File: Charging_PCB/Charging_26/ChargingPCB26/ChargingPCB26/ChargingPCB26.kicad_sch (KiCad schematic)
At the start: 48 parts, among them J1 Molex6pin, J2 Molex6pin, K101 Relay_SPDT_Omron_G2RL-1, K102 Relay_SPDT_Omron_G2RL-1, Q1 NMOS, Q103 Q_NPN_BEC, Q104 Q_NPN_BEC, Q105 Q_NPN_BEC, Q106 Q_NPN_BEC, Q2 NMOS, SW101 SW_Omron_B3FS, SW102 SW_Omron_B3FS, U1 SFH617A-1, U107 LM7805_TO220, U2 SFH617A-1, U5 74LS279, U6 74HC00

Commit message: charging pcb layout
charging pcb ready to order, would like funny logo on there
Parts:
- added D3: LED, LED_SMD:LED_0805_2012Metric_Pad1.15x1.40mm_HandSolder, symbol Device:LED
- added D4: D_Schottky, Diode_SMD:D_SMA, symbol Device:D_Schottky
- added Q3, Q4: NMOS, Package_TO_SOT_THT:TO-251-3_Vertical, symbol Simulation_SPICE:NMOS
- added R10, R8: 10k, Resistor_SMD:R_0805_2012Metric_Pad1.20x1.40mm_HandSolder, symbol Device:R_US
- added R11, R12: 100, Resistor_SMD:R_0805_2012Metric_Pad1.20x1.40mm_HandSolder, symbol Device:R_US
- added R7: 1k, Resistor_SMD:R_0805_2012Metric_Pad1.20x1.40mm_HandSolder, symbol Device:R_US
- added R9: 500, Resistor_SMD:R_0805_2012Metric_Pad1.20x1.40mm_HandSolder, symbol Device:R_US
- C101, C102, C106: footprint Capacitor_THT:CP_Radial_D5.0mm_P2.50mm -> Capacitor_SMD:C_0402_1005Metric; JLC# (none) -> C15195; MPN (none) -> CL05B103KB5NNNC
- C105: footprint Capacitor_THT:CP_Radial_D5.0mm_P2.50mm -> Capacitor_SMD:C_0402_1005Metric; JLC# (none) -> C107013; MPN (none) -> CC0402KRX5R6BB334
- C117, C3: footprint Capacitor_THT:CP_Radial_D5.0mm_P2.50mm -> Capacitor_SMD:C_0603_1608Metric_Pad1.08x0.95mm_HandSolder; JLC# (none) -> C1591; MPN (none) -> CL10B104KB8NNNC
- D1, D2: footprint LED_THT:LED_D3.0mm -> LED_SMD:LED_0805_2012Metric_Pad1.15x1.40mm_HandSolder; JLC# (none) -> C84256; MPN (none) -> NCD0805R1
- D101, D102: footprint Diode_THT:D_DO-201AD_P12.70mm_Horizontal -> Diode_SMD:D_SMA; JLC# (none) -> C8678; MPN (none) -> SS34
- F1: footprint (none) -> Fuse:Fuseholder_Blade_Mini_Keystone_3568; Digikey (none) -> 36-3568-ND
- H101, H102, H103, H104: footprint (none) -> MountingHole:MountingHole_2.2mm_M2
- J1, J2: footprint Connector_Molex:Molex_Mini-Fit_Jr_5566-06A_2x03_P4.20mm_Vertical -> Connector_Molex:Molex_Nano-Fit_105314-xx06_2x03_P2.50mm_Horizontal; JLC# (none) -> C586245; MPN (none) -> 1053141106
- K101, K102: JLC# (none) -> C469130; MPN (none) -> G2RL-1-DC12
- Q1, Q2: JLC# (none) -> C3278986; MPN (none) -> IPU60R2K1CEAKMA1
- Q103, Q104, Q105, Q106: footprint Package_TO_SOT_THT:TO-92 -> Package_TO_SOT_SMD:SOT-23; JLC# (none) -> C2146; MPN (none) -> S8050 J3Y(RANGE:200-350)
- R1, R105, R106, R2: footprint Resistor_THT:R_Axial_DIN0207_L6.3mm_D2.5mm_P7.62mm_Horizontal -> Resistor_SMD:R_0805_2012Metric_Pad1.20x1.40mm_HandSolder; JLC# (none) -> C17414; MPN (none) -> 0805W8F1002T5E
- R103, R104, R110, R112: footprint Resistor_THT:R_Axial_DIN0207_L6.3mm_D2.5mm_P7.62mm_Horizontal -> Resistor_SMD:R_0805_2012Metric_Pad1.20x1.40mm_HandSolder; JLC# (none) -> C149504; MPN (none) -> 0805W8F1003T5E
- R108, R109, R111, R113: footprint Resistor_THT:R_Axial_DIN0207_L6.3mm_D2.5mm_P7.62mm_Horizontal -> Resistor_SMD:R_0805_2012Metric_Pad1.20x1.40mm_HandSolder; JLC# (none) -> C17513; MPN (none) -> 0805W8F1001T5E
- R3, R4: value 2k -> 500; footprint Resistor_THT:R_Axial_DIN0207_L6.3mm_D2.5mm_P7.62mm_Horizontal -> Resistor_SMD:R_0805_2012Metric_Pad1.20x1.40mm_HandSolder; JLC# (none) -> C2828711; MPN (none) -> ARG05BTC5000
- R5, R6: value 10k -> 1k; footprint Resistor_THT:R_Axial_DIN0207_L6.3mm_D2.5mm_P7.62mm_Horizontal -> Resistor_SMD:R_0805_2012Metric_Pad1.20x1.40mm_HandSolder; JLC# (none) -> C17513; MPN (none) -> 0805W8F1001T5E
- SW101, SW102: footprint Button_Switch_THT:SW_PUSH_6mm_H4.3mm -> Button_Switch_SMD:SW_SPST_Omron_B3FS-100xP; JLC# (none) -> C271750; MPN (none) -> B3FS-1000P
- U1, U2: JLC# (none) -> C5350; MPN (none) -> PC817X2NSZW
- U107: JLC# (none) -> C71107; MPN (none) -> LM7805L-TF3-T
- U5: JLC# (none) -> C41430933; MPN (none) -> SN74LS279AN
- U6: JLC# (none) -> C2902; MPN (none) -> SN74HC00N
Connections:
- net +12V: now also D4.1 (K), R7.1
- net +5V: now also R9.1
- net BMS_CSO: now also R7.2
- net GND: now also J2.4 (Pin_4), Q3.3 (S), Q4.3 (S), R10.2, R8.2; no longer J1.4 (Pin_4)
- net +12_Shutdown renamed Charger_SHDN
- net Charger_SHDN: now also R10.1, R11.1, R12.1, R8.1
- new net: D3.1 (K), Q3.1 (D)
- new net: Q3.2 (G), R12.2
- new net: D3.2 (A), R9.2
- new net: Q4.2 (G), R11.2
- new net -12V_Contactor: D4.2 (A), J1.4 (Pin_4), Q4.1 (D)
- no-connect marks 17 -> 16
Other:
- note added: "Power Connections"
- note added: "Signal Connections/Accumulator Power"
- moved on the sheet: C101, C102, C105, C106, C117, C3, D1, D101, D102, D2, F1, H101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

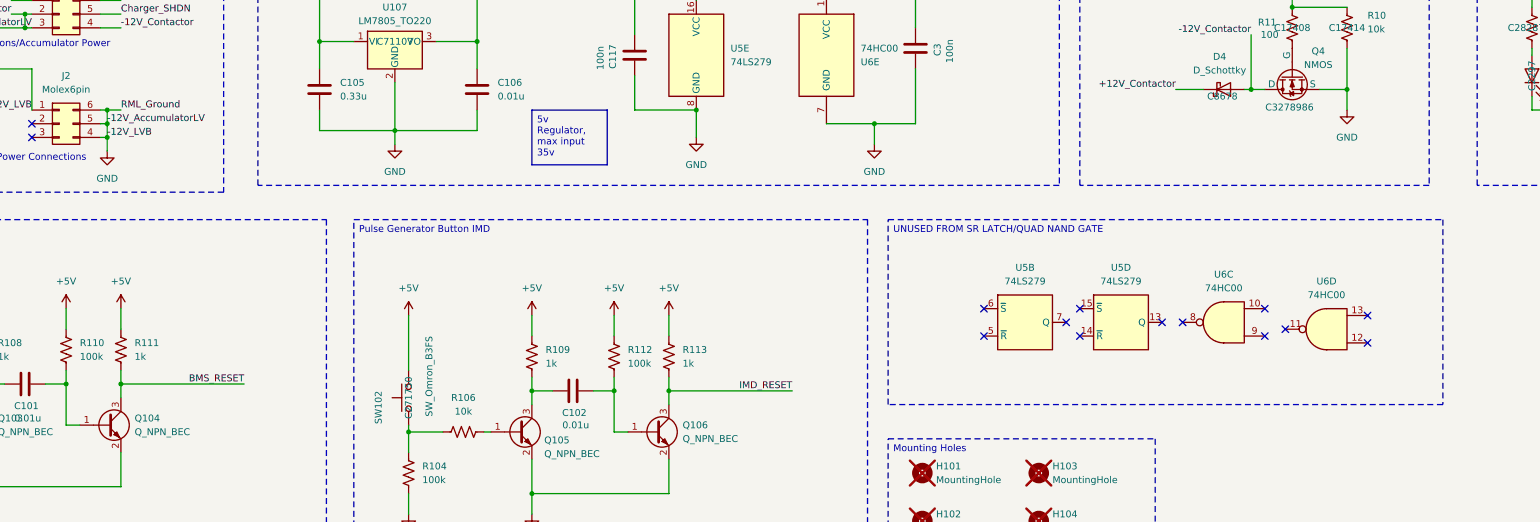
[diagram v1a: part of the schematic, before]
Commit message: charging pcb
terminated unused SR latch/Nand gate inputs
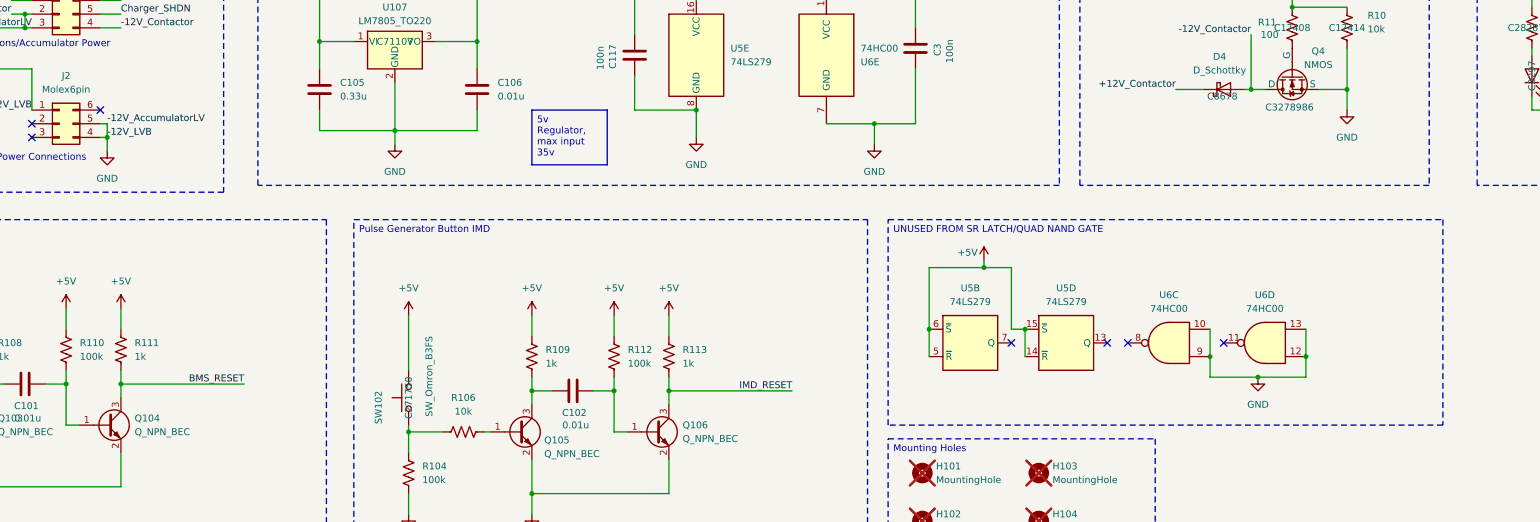
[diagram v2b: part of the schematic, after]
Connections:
- net +5V: now also U5.14 (~{R}), U5.15 (~{S}), U5.5 (~{R}), U5.6 (~{S})
- net GND: now also U6.10, U6.12, U6.13, U6.9; no longer J2.6 (Pin_6)
- no-connect marks 16 -> 9
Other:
- moved on the sheet: U5B, U5D, U6C, U6D

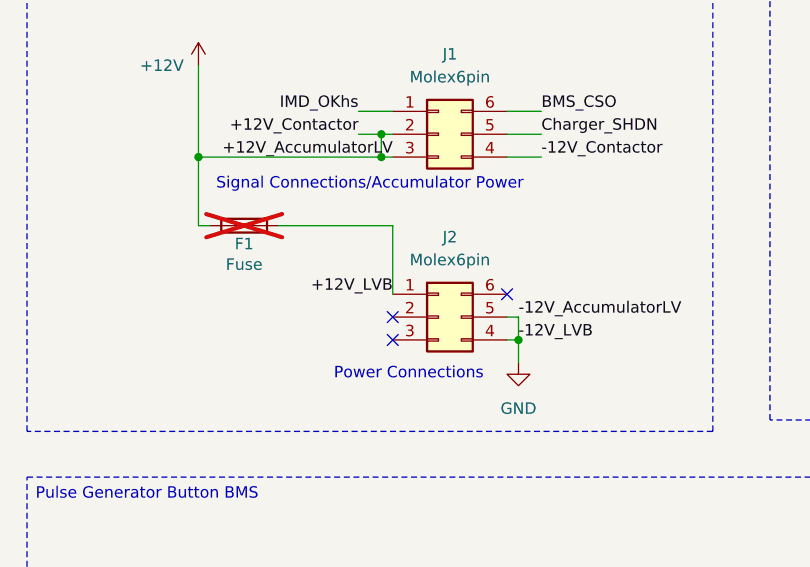
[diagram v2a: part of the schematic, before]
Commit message: precharge/discharge. charging
removed discharge ffrom precharge and put it on board out of battery, updqted charging according to discharge
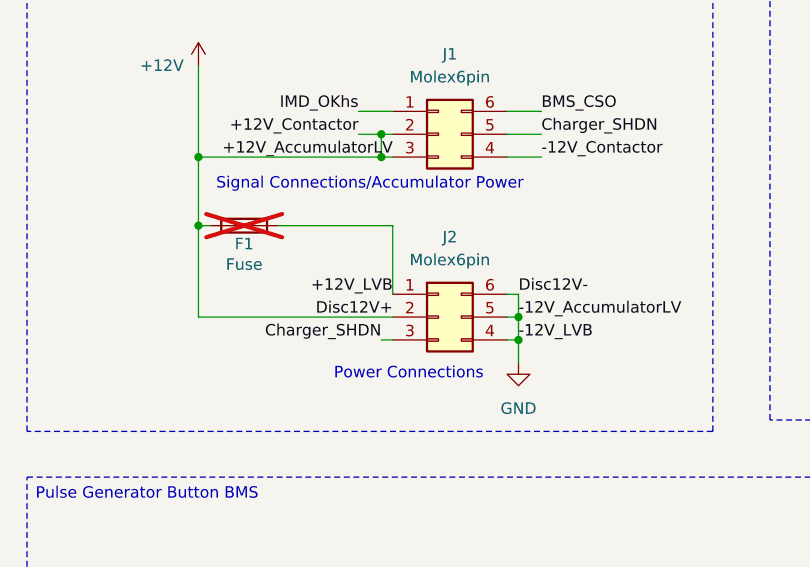
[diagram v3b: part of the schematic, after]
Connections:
- net +12V: now also J2.2 (Pin_2)
- net Charger_SHDN: now also J2.3 (Pin_3)
- net GND: now also J2.6 (Pin_6)
- no-connect marks 9 -> 6
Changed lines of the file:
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@@
 	)
 	(junction
+		(at 85.09 215.9)
+		(diameter 0)
+		(color 0 0 0 0)
+	)
+	(junction
 		(at 105.41 100.33)
 		(diameter 0)
@@
 	)
 	(junction
+		(at 49.53 205.74)
+		(diameter 0)
+		(color 0 0 0 0)
+	)
+	(junction
 		(at 237.49 254)
 		(diameter 0)
@@
 	)
 	(no_connect
-		(at 71.12 218.44)
-	)
-	(no_connect
 		(at 320.04 138.43)
 	)
@@
 	)
 	(no_connect
-		(at 71.12 215.9)
-	)
-	(no_connect
-		(at 83.82 213.36)
-	)
-	(no_connect
 		(at 292.1 256.54)
 	)
@@
 	(wire
 		(pts
+			(xy 71.12 215.9) (xy 49.53 215.9)
+		)
+		(stroke
+			(width 0)
+			(type default)
+		)
+	)
+	(wire
+		(pts
 			(xy 138.43 217.17) (xy 138.43 219.71)
 		)
@@
 	(wire
 		(pts
+			(xy 69.85 218.44) (xy 71.12 218.44)
+		)
+		(stroke
+			(width 0)
+			(type default)
+		)
+	)
+	(wire
+		(pts
+			(xy 85.09 213.36) (xy 85.09 215.9)
+		)
+		(stroke
+			(width 0)
+			(type default)
+		)
+	)
+	(wire
+		(pts
 			(xy 317.5 118.11) (xy 323.85 118.11)
 		)
@@
 	(wire
 		(pts
+			(xy 83.82 213.36) (xy 85.09 213.36)
+		)
+		(stroke
+			(width 0)
+			(type default)
+		)
+	)
+	(wire
+		(pts
 			(xy 234.95 205.74) (xy 234.95 215.9)
 		)
@@
 	(wire
 		(pts
+			(xy 49.53 215.9) (xy 49.53 205.74)
+		)
+		(stroke
+			(width 0)
+			(type default)
+		)
+	)
+	(wire
+		(pts
 			(xy 317.5 130.81) (xy 317.5 118.11)
 		)
@@
 		)
 	)
+	(label "Charger_SHDN"
+		(at 69.85 218.44 180)
+		(effects
+			(font
+				(size 1.27 1.27)
+			)
+			(justify right bottom)
+		)
+	)
 	(label "+12V_Contactor"
 		(at 283.21 209.55 180)
@@
 		)
 	)
+	(label "Disc12V+"
+		(at 71.12 215.9 180)
+		(effects
+			(font
+				(size 1.27 1.27)
+			)
+			(justify right bottom)
+		)
+	)
 	(label "IMD_RESET"
 		(at 212.09 265.43 180)
@@
 		(effects
 			(font
+				(size 1.27 1.27)
+			)
+			(justify left bottom)
+		)
+	)
+	(label "Disc12V-"
+		(at 85.09 213.36 0)
+		(effects
+			(font

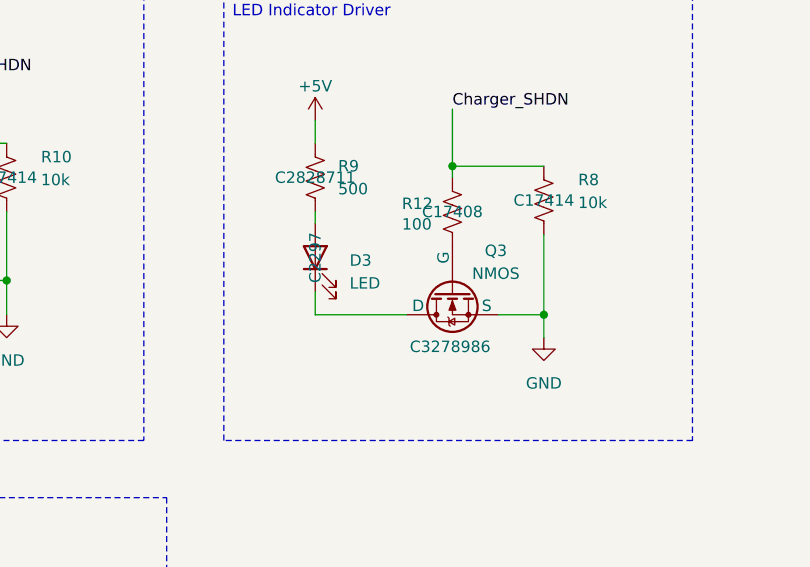
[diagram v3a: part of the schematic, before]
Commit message: BSPD, Precharge, and Charging PCB BOMs pulled
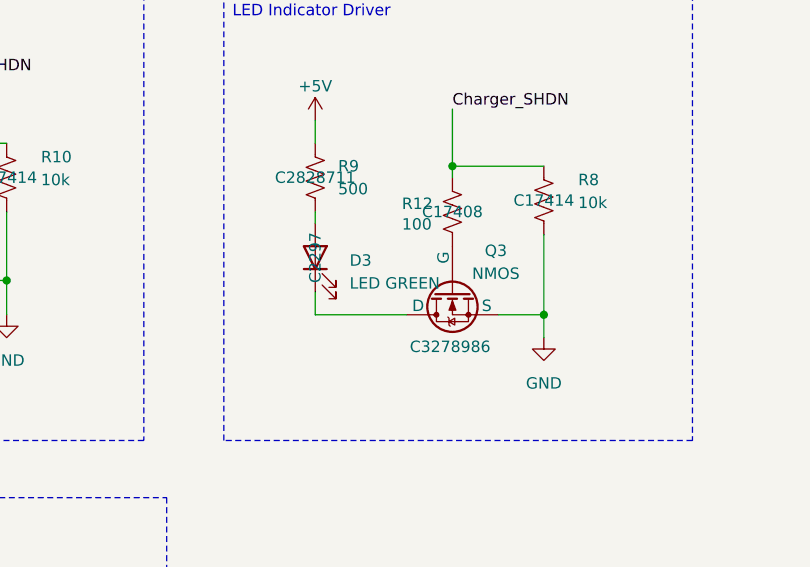
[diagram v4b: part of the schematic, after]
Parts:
- D3: value LED -> LED GREEN; Digikey 516-1313-ND -> (none)
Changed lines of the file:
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@@
 			"AAAAAAAAAAAAAAAAAAAAAAAAAAAAAAAAAAAAAAAAAAAAAAAAAAAAAAAAAAAAAAAAAAAAAAAAAAAA"
 			"AAAAAAAAAAAAAAAAAAAAAAAAAAAAAAAAAAAAAAAAAAAAAAAAAAAAAAAAAAAAAAAAAAAAAAAAAAAA"
+			"AAAAAAAAAAAAAAAAAAAAAAAAAAAAAAAAAAAAAAAAAAAAAAAAAAAAAAAAAAAAAAAAAAAAAAAAAAAA"
+			"AAAAAAAAAAAAAAAAAAAAAAAAAAAAAAAAAAAAAAAAAAAAAAAAAAAAAAAAAAAAAAAAAAAAAAAAAAAA"
+			"AAAAAAAAAAAAAAAAAAAAAAAAAAAAAAAAAAAAAAAAAAAAAAAAAAAAAAAAAAAAAAAAAAAAAAAAAAAA"
+			"AAAAAAAAAAAAAAAAAAAAAAAAAAAAAAAAAAAAAAAAAAAAAAAAAAAAAAAAAAAAAAAAAAAAAAAAAAAA"
+			"AAAAAAAAAAAAAAAAAAAAAAAAAAAAAAAAAAAAAAAAAAAAAAAAAAAAAAAAAAAAAAAAAAAAAAAAAAAA"
+			"AAAAAAAAAAAAAAAAAAAAAAAAAAAAAAAAAAAAAAAAAAAAAAAAAAAAAAAAAAAAAAAAAAAAAAAAAAAA"
+			"AAAAAAAAAAAAAAAAAAAAAAAAAAAAAAAAAAAAAAAAAAAAAAAAAAAAAAAAAAAAAAAAAAAAAAAAAAAA"
+			"AAAAAAAAAAAAAAAAAAAAAAAAAAAAAAAAAAAAAAAAAAAAAAAAAAAAAAAAAAAAAAAAAAAAAAAAAAAA"
+			"AAAAAAAAAAAAAAAAAAAAAAAAAAAAAAAAAAAAAAAAAAAAAAAAAAAAAAAAAAAAAAAAAAAAAAAAAAAA"
+			"AAAAAAAAAAAAAAAAAAAAAAAAAAAAAAAAAAAAAAAAAAAAAAAAAAAAAAAAAAAAAAAAAAAAAAAAAAAA"
+			"AAAAAAAAAAAAAAAAAAAAAAAAAAAAAAAAAAAAAAAAAAAAAAAAAAAAAAAAAAAAAAAAAAAAAAAAAAAA"
+			"AAAAAAAAAAAAAAAAAAAAAAAAAAAAAAAAAAAAAAAAAAAAAAAAAAAAAAAAAAAAAAAAAAAAAAAAAAAA"
+			"AAAAAAAAAAAAAAAAAAAAAAAAAAAAAAAAAAAAAAAAAAAAAAAAAAAAAAAAAAAAAAAAAAAAAAAAAAAA"
+			"AAAAAAAAAAAAAAAAAAAAAAAAAAAAAAAAAAAAAAAAAAAAAAAAAAAAAAAAAAAAAAAAAAAAAAAAAAAA"
+			"AAAAAAAAAAAAAAAAAAAAAAAAAAAAAAAAAAAAAAAAAAAAAAAAAAAAAAAAAAAAAAAAAAAAAAAAAAAA"
+			"AAAAAAAAAAAAAAAAAAAAAAAAAAAAAAAAAAAAAAAAAAAAAAAAAAAAAAAAAAAAAAAAAAAAAAAAAAAA"
+			"AAAAAAAAAAAAAAAAAAAAAAAAAAAAAAAAAAAAAAAAAAAAAAAAAAAAAAAAAAAAAAAAAAAAAAAAAAAA"
+			"AAAAAAAAAAAAAAAAAAAAAAAAAAAAAAAAAAAAAAAAAAAAAAAAAAAAAAAAAAAAAAAAAAAAAAAAAAAA"
 			"AAAAAAAAAAAAAA=="
 		)
@@
 			"AAAAAAAAAAAAAAAAAAAAAAAAAAAAAAAAAAAAAAAAAAAAAAAAAAAAAAAAAAAAAAAAAAAAAAAAAAAA"
 			"AAAAAAAAAAAAAAAAAAAAAAAAAAAAAAAAAAAAAAAAAAAAAAAAAAAAAAAAAAAAAAAAAAAAAAAAAAAA"
+			"AAAAAAAAAAAAAAAAAAAAAAAAAAAAAAAAAAAAAAAAAAAAAAAAAAAAAAAAAAAAAAAAAAAAAAAAAAAA"
+			"AAAAAAAAAAAAAAAAAAAAAAAAAAAAAAAAAAAAAAAAAAAAAAAAAAAAAAAAAAAAAAAAAAAAAAAAAAAA"
+			"AAAAAAAAAAAAAAAAAAAAAAAAAAAAAAAAAAAAAAAAAAAAAAAAAAAAAAAAAAAAAAAAAAAAAAAAAAAA"
+			"AAAAAAAAAAAAAAAAAAAAAAAAAAAAAAAAAAAAAAAAAAAAAAAAAAAAAAAAAAAAAAAAAAAAAAAAAAAA"
+			"AAAAAAAAAAAAAAAAAAAAAAAAAAAAAAAAAAAAAAAAAAAAAAAAAAAAAAAAAAAAAAAAAAAAAAAAAAAA"
+			"AAAAAAAAAAAAAAAAAAAAAAAAAAAAAAAAAAAAAAAAAAAAAAAAAAAAAAAAAAAAAAAAAAAAAAAAAAAA"
+			"AAAAAAAAAAAAAAAAAAAAAAAAAAAAAAAAAAAAAAAAAAAAAAAAAAAAAAAAAAAAAAAAAAAAAAAAAAAA"
+			"AAAAAAAAAAAAAAAAAAAAAAAAAAAAAAAAAAAAAAAAAAAAAAAAAAAAAAAAAAAAAAAAAAAAAAAAAAAA"
+			"AAAAAAAAAAAAAAAAAAAAAAAAAAAAAAAAAAAAAAAAAAAAAAAAAAAAAAAAAAAAAAAAAAAAAAAAAAAA"
+			"AAAAAAAAAAAAAAAAAAAAAAAAAAAAAAAAAAAAAAAAAAAAAAAAAAAAAAAAAAAAAAAAAAAAAAAAAAAA"
+			"AAAAAAAAAAAAAAAAAAAAAAAAAAAAAAAAAAAAAAAAAAAAAAAAAAAAAAAAAAAAAAAAAAAAAAAAAAAA"
+			"AAAAAAAAAAAAAAAAAAAAAAAAAAAAAAAAAAAAAAAAAAAAAAAAAAAAAAAAAAAAAAAAAAAAAAAAAAAA"
+			"AAAAAAAAAAAAAAAAAAAAAAAAAAAAAAAAAAAAAAAAAAAAAAAAAAAAAAAAAAAAAAAAAAAAAAAAAAAA"
+			"AAAAAAAAAAAAAAAAAAAAAAAAAAAAAAAAAAAAAAAAAAAAAAAAAAAAAAAAAAAAAAAAAAAAAAAAAAAA"
+			"AAAAAAAAAAAAAAAAAAAAAAAAAAAAAAAAAAAAAAAAAAAAAAAAAAAAAAAAAAAAAAAAAAAAAAAAAAAA"
+			"AAAAAAAAAAAAAAAAAAAAAAAAAAAAAAAAAAAAAAAAAAAAAAAAAAAAAAAAAAAAAAAAAAAAAAAAAAAA"
+			"AAAAAAAAAAAAAAAAAAAAAAAAAAAAAAAAAAAAAAAAAAAAAAAAAAAAAAAAAAAAAAAAAAAAAAAAAAAA"
+			"AAAAAAAAAAAAAAAAAAAAAAAAAAAAAAAAAAAAAAAAAAAAAAAAAAAAAAAAAAAAAAAAAAAAAAAAAAAA"
 			"AAAAAAAAAAAAAAAAAAAAAAAAAAAAAAAAAAAAAAAAAAAAAAAAAA=="
 		)
@@
 			"91MLSQi+nYNccT/G+3YbTolYDR85JiJ7BvnoF99fAJ70TTs3ay1gIiL6LDFkJVqv5WZyonXpd7sD"
 			"NhnRigz63T44RxERERliyEpEREREREQbitMvERERERER0YZiyEpEREREREQbiiErERERERERbSiG"
-			"rERERERERLShGLISERERERHRhvr/QPPDmXRA+L0AAAAASUVORK5CYII="
+			"rERERERERLShGLISERERERHRhvr/QPPDmXRA+L0AAAAASUVORK5CYIJiMmRnQkFTVW5KRHovOGdM"
+			"MUx4amZEZ29JQ2IyOXZUMDlQTVRHeEowK2V3TDZ2Vi84cEtDZ3dNRERJeU1nWVAzNThhMnVyaUln"
+			"SW9ZVWNEc2ZMeTJ2NTh1VTFOVFgxOWZWV1ZsYndlVTU0TjQ2SWlMQ3hzV0d4V0RvNk9pMHRMVXdt"
+			"azhsa01oZ01VVkZSSnBOSjFqOElVeEVRZ2Y2QjBBWnNYUmNVRk96Y3VYUDc5dTN5OHZJSER4NzA4"
+			"UERZdG0yYnJLenN5Wk1uWVNtaC9RTlozdkZWUU1qUW9VTUZRdHJhMmpvN084K2NPUk1hR3RyYTJr"
+			"cDRWbmQzOTZaTm0yQno4L1B6MjdScFUwOVBEd0RBMzk4L016TVR4dkh5OHFxcHFhbXJxN08ydHE2"
+			"dHJRVkVqWUxNZUJUQ0dpUnIrQkI4bjROTkVOL0o1T2ZuSHpwMHlOWFZGV2IyM0xselM1WXN5YzNO"
+			"Yldob3NMVzFkWGQzejhuSmFXdHJtenAxS3JiMjBmSUhBRGc0T0h6NjlHbkNoQW13ZC8zYUlIMEIz"
+			"cklWRnhmRGYyTmlZaVFrSkdwcmF4RUUrZkRoQXdDZ3FxcXFvNk5EVGs2dXNMQVF4dEhSMFhudzRB"
+			"R2FncCtmbjQyTlRVOVBEeG9DZTBuc1ZmaDgvcU5IajRZT0hZb2dDSmZMeFY3UnlNZ29MQ3dNSG50"
+			"N2U3dTd1eE9tQ1RsNDhLQ1ptUms4N3VycWtwS1N1bnYzTGx4Y1VGbFpDY1BOek15dVg3K09JRWg4"
+			"ZlB5WU1XTmdZSFIwdElpSVNHNXVMdnpYMGRIUnc4TURRWkR0Mjdldlc3Y09Cc0lSQW0raFFFRmxa"
+			"bWJLeXNyQ0lzTFMyZGtwTFMzOTRzVUwrTy9XclZ1aHFiLzk5dHVxVmF0ZzRNMmJOMDFNVEJBRVdi"
+			"aHc0YTVkdTlCelkySmlvS2tIRGh4d2NIQ0FnWldWbFV3bUV5Wm9ZV0d4YmRzMkdMNTgrWEpQVDAv"
+			"Q2xNbHN3TlBZMkNnaElaR1ZsVVdXSFJRT2grUHI2K3ZrNUlRZ2lJK1BqNUdSRVkvSFF4RGt5cFVy"
+			"MnRyYTJKaUV0WU1neU9USmsxMWRYV0g0NjlldkdReEdXVmtaWWJGUXAzLzgrSEZMUzBzK240K0d6"
+			"Snc1MDl2Ykd4NC9mLzVjVkZTMHBxWUdyU24wZ05DQlg3OStMWkJ4YkwxM2RYVkpTMHRIUlVYQm4z"
+			"Nzc3VGNEQXdNRVFYYnQyalZxMUtqT3prNnNZVUtlcUs2dTN0WFZoU0JJVDArUHZMeDhTRWhJY25L"
+			"eXFLaG9jM016akR4anhveXRXN2NpQ09McjZ3c0xoekNEaVltSmlvcQ=="
 		)
 	)
@@
 			"AHcAcwA5AHoATQBLAHQAagB4ADQANgB4ADIAVwB6ADQAUwBjAHYAWgAyAGIAbQB3AHMAQgBDAE8A"
 			"ZgA0AEkAVQBGAGgAWgBxAGEAVwBuAE4AbgBEAGsAVABsADgAbQAzADMAMwA0AEwAQQBJAEQAegAr"
-			"AHQARwBzAFkASg=="
+			"AHQARwBzAFkASgBhADIAdAB2AEIAMwBXADEAcwBiAEEARwBEAFEAbwBFAEcAZgA1AHQAWQBrAEoA"
+			"QwBRADkAQQAyAHUAMgBYAHoARgB0AGIAVwAyAEcAaABvAFoAawAyAE4AcQB2ACsAUgAvAFIAVgBS"
+			"AEkAcwBaAEsAWAAzAEgAaQBFAHoAdABNAHIATAB5ADkAMwBjADMASgBoAE0ANQBvAEEAQgBBAC8A"
+			"egA4AC8ATwByAHEANgB0AEIAVABmAEQANAAvAFAARAB4ADgAMQBLAGgAUgBDAGcAbwBLAGQARABy"
+			"AGQAegBNAHcAcwBJAEMAQQBBAE4AMwBvAFMANQBkADkALwAvAC8AWAB5ADgAdQBKAHcATwBIAEoA"
+			"eQBjAGkAbwBxAEsAcwA3AE8AegBuAGYAdQAzAEUASAB6ADQAWABLADUAcAAwADYAZABPAG4AbgB5"
+			"AHAASwBXAGwASgBZAFAAQgBNAEQASQB5ADIAcgBGAGoAQgA1AC8AUABSAHkAOAB2AEsAQwBpAFkA"
+			"UABYAHYAMgBnAEEARQBEAEYAQgBRAFUAYgBHADEAdAB6ADUAOAAvAEQANAAvAG4ANQB1AFoAeQB1"
+			"AFYAdwA0AEsARABBAG4ASgA0AGYATAA1AGUAYgBrADUAQQBRAEUAQgBPAGoAcAA2AFQARQBZAGoA"
+			"SwBGAEQAaAA4AGIASAB4ADIAUABGAHUASABuAHoAcABvAE8ARABnADQASwBDAGcAcQBhAG0ANQBw"
+			"AG8AMQBhADYANQBkAHUAOABiAGwAYwBwADgAOABlAFMASgBKADYAYwBUAEcAeABuAEsANQAzAEsA"
+			"cQBxAHEAdgBuAHoANQB3AGMARwBCAGcASQBBADEAcQAxAGIAeAArAFYAeQBTADAAdABMAGMAUwBt"
+			"AG4AVABKAGsAQwBPADIAVwA1AFgATwA3AHUAMwBiAHYAUgA0ADMAZgB2ADMAbgBWAHcAYwBHAEEA"
+			"eQBtAGUAcgBxADYAagA0ACsAUABtAC8AZQB2AEUARgBQAEkAUQBnAFMARwBSAGwAcABiAFcAMwBO"
+			"AFkARABBADAATgBEAFMAOAB2AEwAegBFAHYAawAvADMAcgBHAHAAKwArAGUAVwBYAHcANABjAFAA"
+			"QQB3AEIAOABmAEgAdwA4AFAAVAAwAFQARQBoAEwAZwBOAHMAbwBSAEUAUgBGAGMATABoAGQAbQBR"
+			"AGkAQgBNAFIAMABjAEgAbAA4AHUATgBpADQAdABiAHMAVwBJAEYAaQA4AFUAYQBPAFgASgBrAFIA"
+			"awBZAEcAcgBEADYAcwBiAE4AbgBaADIAVgB3AHUARgAzADcAMAB3AFEATAByAEsARABNAHoAYwAv"
+			"AEgAaQB4AGEAcQ=="
 		)
 	)
@@
 			)
 		)
-		(property "Value" "LED"
+		(property "Value" "LED GREEN"
 			(at 353.06 209.8674 90)
 			(effects
@@
 			)
 		)
-		(property "Digikey" "516-1313-ND"
+		(property "Digikey" ""
 			(at 349.25 207.01 90)
 			(effects
